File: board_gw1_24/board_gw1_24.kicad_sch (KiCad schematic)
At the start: 147 parts, among them J1 USB_C_Receptacle, Q10 2N7002, Q14 2N7002, Q15 2N7002, Q19 2N7002, Q2 2N7002, Q20 2N7002, Q25 2N7002, Q26 2N7002, Q28 2N7002, Q29 2N7002, Q3 2N7002, Q30 2N7002, Q32 2N7002, Q33 2N7002, Q34 2N7002, Q35 2N7002, Q36 2N7002, Q38 2N7002, Q39 2N7002, Q41 2N7002, Q5 2N7002, Q6 2N7002, Q7 2N7002, Q8 2N7002, Q9 2N7002, U1 GW1NR-LV9-QN88-C6/I5, U11 FT232H, U2 ESD224DQA, U3 MIC5203-3.3BM5, U4 APS6404L-3SQR-ZR, U5 MIC5504-1.2YM5, U6 TPS562242, U7 W25Q16JVUXIQ, X1 12MHz

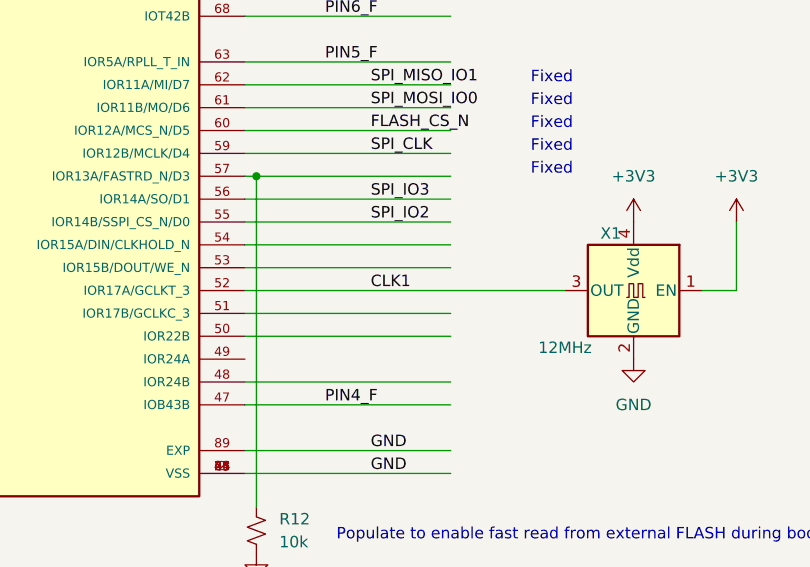
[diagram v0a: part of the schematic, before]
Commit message: Cleaned up some shapes, added series resistor to clock.
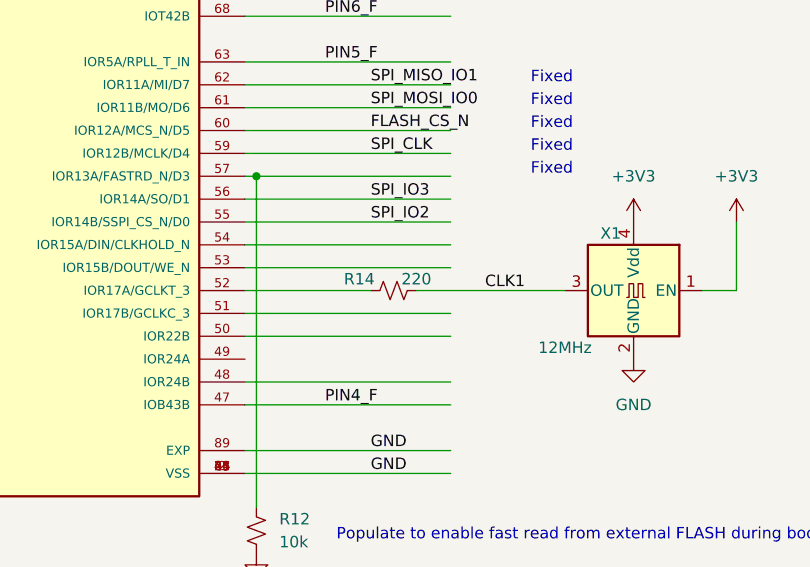
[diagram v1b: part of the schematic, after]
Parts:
- added R14: 220, Resistor_SMD:R_0201_0603Metric, symbol Device:R_Small_US
- X1: footprint UNIC:Oscillator_SMD_Abracon_ASE-4Pin_3.2x2.5mm -> UNIC:Oscillator_SMD_2.5x2.0mm; manufacturer (none) -> EPSON; mpn (none) -> SG-210STF 12.0000ML5
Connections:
- net CLK1: now also R14.2; no longer U1.52 (IOR17A/GCLKT_3)
- new net: R14.1, U1.52 (IOR17A/GCLKT_3)
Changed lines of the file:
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@@
 	(wire
 		(pts
-			(xy 168.91 146.05) (xy 204.47 146.05)
+			(xy 168.91 146.05) (xy 182.88 146.05)
 		)
 		(stroke
@@
 	(wire
 		(pts
+			(xy 187.96 146.05) (xy 204.47 146.05)
+		)
+		(stroke
+			(width 0)
+			(type default)
+		)
+	)
+	(wire
+		(pts
 			(xy 198.12 209.55) (xy 200.66 209.55)
 		)
@@
 	)
 	(label "CLK1"
-		(at 182.88 146.05 0)
+		(at 195.58 146.05 0)
 		(effects
 			(font
@@
 	)
 	(symbol
+		(lib_id "Device:R_Small_US")
+		(at 185.42 146.05 90)
+		(unit 1)
+		(exclude_from_sim no)
+		(in_bom yes)
+		(on_board yes)
+		(dnp no)
+		(property "Reference" "R14"
+			(at 181.61 144.78 90)
+			(effects
+				(font
+					(size 1.27 1.27)
+				)
+			)
+		)
+		(property "Value" "220"
+			(at 187.96 144.78 90)
+			(effects
+				(font
+					(size 1.27 1.27)
+				)
+			)
+		)
+		(property "Footprint" "Resistor_SMD:R_0201_0603Metric"
+			(at 185.42 146.05 0)
+			(effects
+				(font
+					(size 1.27 1.27)
+				)
+				(hide yes)
+			)
+		)
+		(property "Datasheet" "~"
+			(at 185.42 146.05 0)
+			(effects
+				(font
+					(size 1.27 1.27)
+				)
+				(hide yes)
+			)
+		)
+		(property "Description" ""
+			(at 185.42 146.05 0)
+			(effects
+				(font
+					(size 1.27 1.27)
+				)
+				(hide yes)
+			)
+		)
+		(property "mpn" ""
+			(at 185.42 146.05 0)
+			(effects
+				(font
+					(size 1.27 1.27)
+				)
+				(hide yes)
+			)
+		)
+		(property "manufacturer" ""
+			(at 185.42 146.05 0)
+			(effects
+				(font
+					(size 1.27 1.27)
+				)
+				(hide yes)
+			)
+		)
+		(property "manf" ""
+			(at 185.42 146.05 0)
+			(effects
+				(font
+					(size 1.27 1.27)
+				)
+				(hide yes)
+			)
+		)
+		(property "manf#" ""
+			(at 185.42 146.05 0)
+			(effects
+				(font
+					(size 1.27 1.27)
+				)
+				(hide yes)
+			)
+		)
+		(property "MP" ""
+			(at 185.42 146.05 0)
+			(effects
+				(font
+					(size 1.27 1.27)
+				)
+				(hide yes)
+			)
+		)
+		(property "SnapEDA_Link" ""
+			(at 185.42 146.05 0)
+			(effects
+				(font
+					(size 1.27 1.27)
+				)
+				(hide yes)
+			)
+		)
+		(pin "1"
+		)
+		(pin "2"
+		)
+		(instances
+			(project "board_gw1_24"
+				(path "/f6df1e3b-3728-4bb2-8d84-c5251d58c11a"
+					(reference "R14")
+					(unit 1)
+				)
+			)
+		)
+	)
+	(symbol
 		(lib_id "power:GND")
 		(at 474.98 44.45 0)
@@
 			)
 		)
-		(property "Footprint" "UNIC:Oscillator_SMD_Abracon_ASE-4Pin_3.2x2.5mm"
+		(property "Footprint" "UNIC:Oscillator_SMD_2.5x2.0mm"
 			(at 194.31 154.94 0)
 			(effects
@@
 			)
 		)
-		(property "mpn" ""
+		(property "mpn" "SG-210STF 12.0000ML5"
 			(at 212.09 146.05 0)
 			(effects
@@
 			)
 		)
-		(property "manufacturer" ""
+		(property "manufacturer" "EPSON"
 			(at 212.09 146.05 0)
 			(effects
